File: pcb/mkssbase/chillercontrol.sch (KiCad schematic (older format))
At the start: 13 parts, among them J17 Switch, J18 PWR IN, J19 PWR OUT, J20 SSR, Q2 BC547, U2 4011

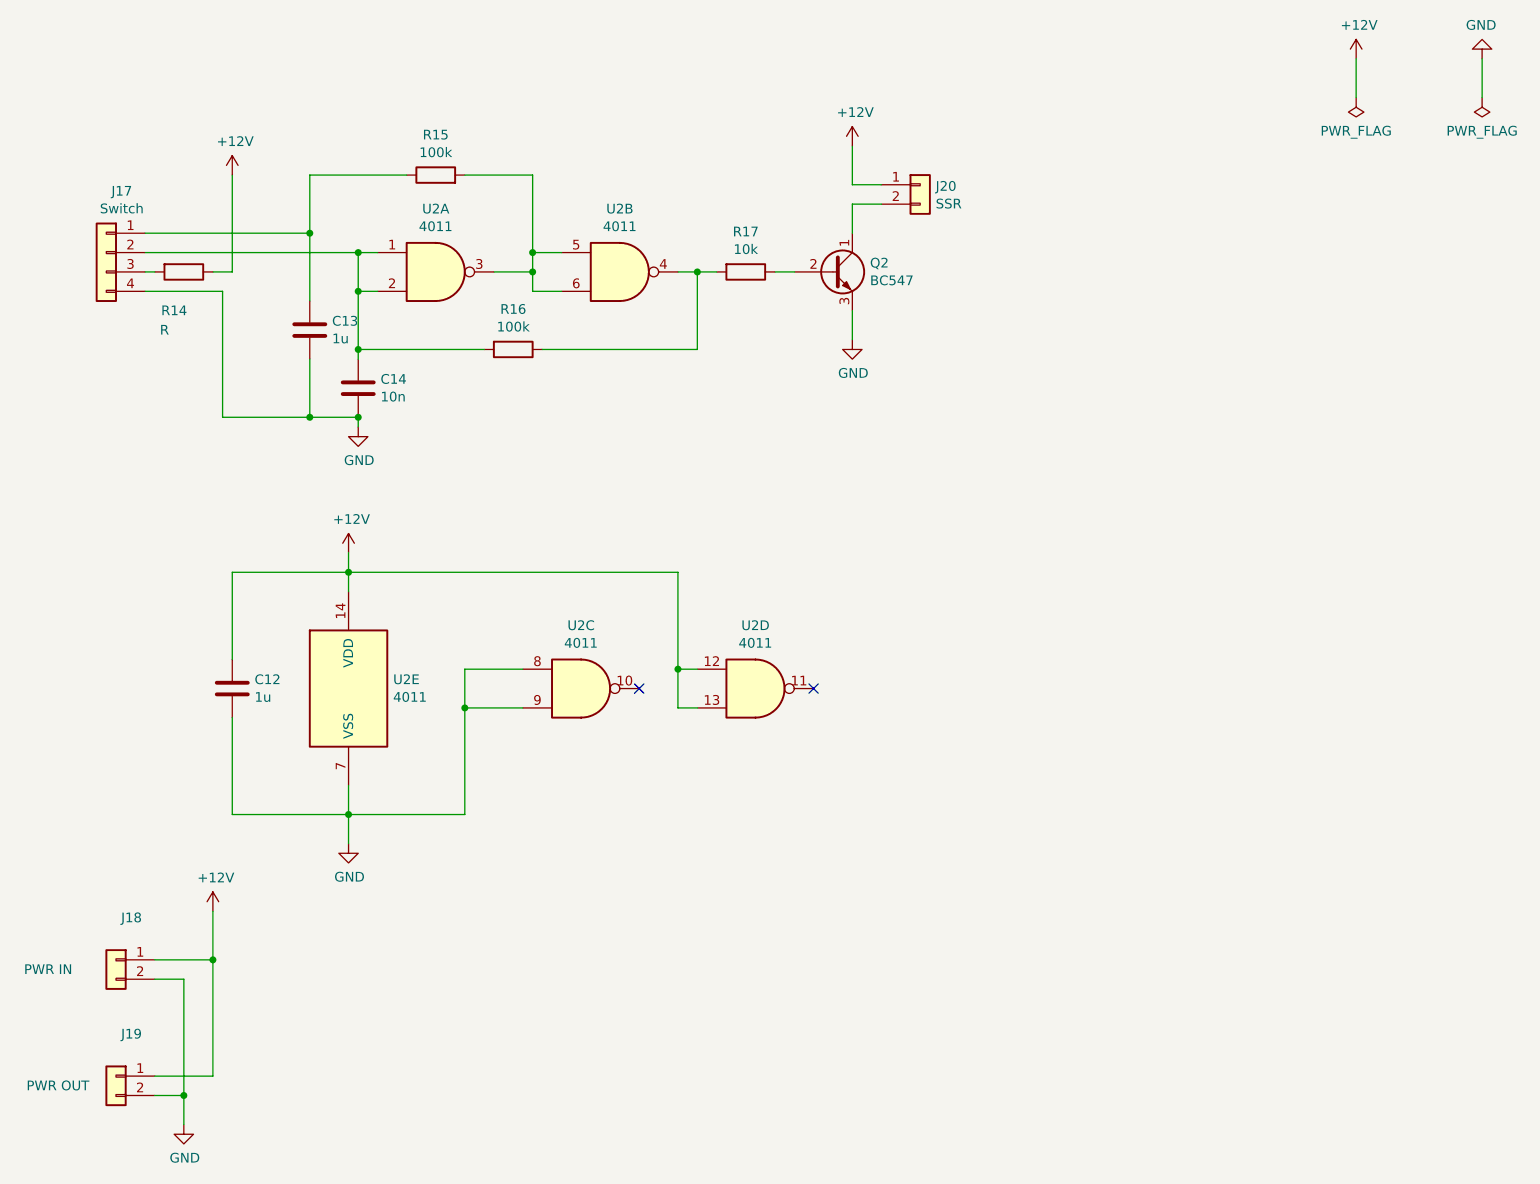
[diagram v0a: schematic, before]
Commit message: Integrate chiller control.
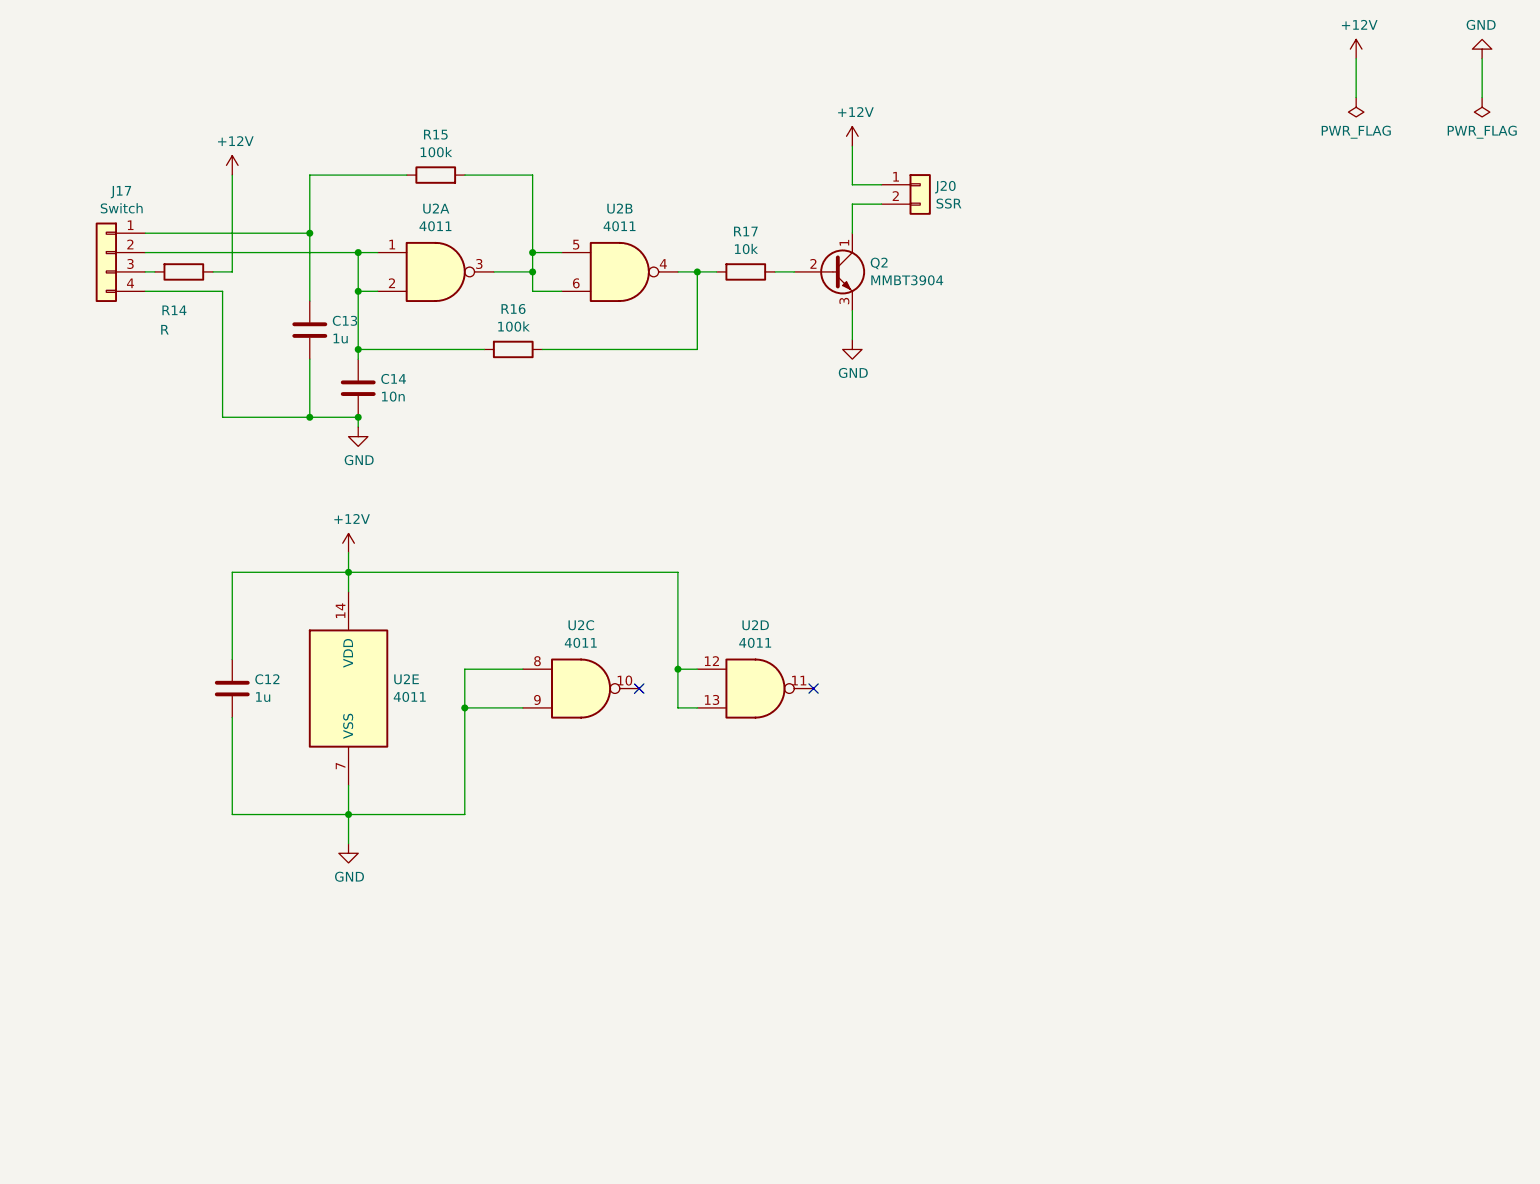
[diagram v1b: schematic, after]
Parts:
- removed J18: PWR IN, Connector_JST:JST_PH_B2B-PH-K_1x02_P2.00mm_Vertical, symbol Connector_Generic:Conn_01x02
- removed J19: PWR OUT, Connector_JST:JST_PH_B2B-PH-K_1x02_P2.00mm_Vertical, symbol Connector_Generic:Conn_01x02
- C12, C13: footprint Capacitor_THT:C_Rect_L7.0mm_W6.0mm_P5.00mm -> Capacitor_SMD:C_0805_2012Metric
- C14: footprint Capacitor_THT:C_Disc_D8.0mm_W2.5mm_P5.00mm -> Capacitor_SMD:C_0603_1608Metric
- Q2: value BC547 -> MMBT3904; footprint Package_TO_SOT_THT:TO-92L_Wide -> Package_TO_SOT_SMD:SOT-23
- R15, R16, R17: footprint Resistor_THT:R_Axial_DIN0207_L6.3mm_D2.5mm_P5.08mm_Vertical -> Resistor_SMD:R_0603_1608Metric
- U2: footprint Package_DIP:DIP-14_W7.62mm_LongPads -> Package_SO:SOIC-14_3.9x8.7mm_P1.27mm
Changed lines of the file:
@@
 EESchema Schematic File Version 4
 LIBS:mkssbase-cache
-LIBS:chillercontrol-cache
 EELAYER 26 0
 EELAYER END
@@
 $EndDescr
 $Comp
-L Connector_Generic:Conn_01x02 J19
-U 1 1 5C59E722
-P 1900 6950
-F 0 "J19" H 1820 7167 50  0000 C CNN
-F 1 "PWR OUT" H 2200 6900 50  0000 C CNN
-F 2 "Connector_JST:JST_PH_B2B-PH-K_1x02_P2.00mm_Vertical" H 1900 6950 50  0001 C CNN
-F 3 "~" H 1900 6950 50  0001 C CNN
-	1    1900 6950
-	-1   0    0    -1
-$EndComp
-$Comp
-L Connector_Generic:Conn_01x02 J18
-U 1 1 5C59E800
-P 1900 6350
-F 0 "J18" H 1820 6567 50  0000 C CNN
-F 1 "PWR IN" H 2250 6300 50  0000 C CNN
-F 2 "Connector_JST:JST_PH_B2B-PH-K_1x02_P2.00mm_Vertical" H 1900 6350 50  0001 C CNN
-F 3 "~" H 1900 6350 50  0001 C CNN
-	1    1900 6350
-	-1   0    0    -1
-$EndComp
-$Comp
 L Connector_Generic:Conn_01x02 J20
 U 1 1 5C59E879
@@
 F 0 "U2" H 4500 3125 50  0000 C CNN
 F 1 "4011" H 4500 3034 50  0000 C CNN
-F 2 "Package_DIP:DIP-14_W7.62mm_LongPads" H 4500 2800 50  0001 C CNN
+F 2 "Package_SO:SOIC-14_3.9x8.7mm_P1.27mm" H 4500 2800 50  0001 C CNN
 F 3 "http://www.intersil.com/content/dam/Intersil/documents/cd40/cd4011bms-12bms-23bms.pdf" H 4500 2800 50  0001 C CNN
 	2    4500 2800
@@
 F 0 "R15" V 3757 2300 50  0000 C CNN
 F 1 "100k" V 3666 2300 50  0000 C CNN
-F 2 "Resistor_THT:R_Axial_DIN0207_L6.3mm_D2.5mm_P5.08mm_Vertical" V 3480 2300 50  0001 C CNN
+F 2 "Resistor_SMD:R_0603_1608Metric" V 3480 2300 50  0001 C CNN
 F 3 "~" H 3550 2300 50  0001 C CNN
 	1    3550 2300
@@
 F 0 "R16" V 3743 3200 50  0000 C CNN
 F 1 "100k" V 3834 3200 50  0000 C CNN
-F 2 "Resistor_THT:R_Axial_DIN0207_L6.3mm_D2.5mm_P5.08mm_Vertical" V 3880 3200 50  0001 C CNN
+F 2 "Resistor_SMD:R_0603_1608Metric" V 3880 3200 50  0001 C CNN
 F 3 "~" H 3950 3200 50  0001 C CNN
 	1    3950 3200
@@
 F 0 "C14" H 3265 3446 50  0000 L CNN
 F 1 "10n" H 3265 3355 50  0000 L CNN
-F 2 "Capacitor_THT:C_Disc_D8.0mm_W2.5mm_P5.00mm" H 3188 3250 50  0001 C CNN
+F 2 "Capacitor_SMD:C_0603_1608Metric" H 3188 3250 50  0001 C CNN
 F 3 "~" H 3150 3400 50  0001 C CNN
 	1    3150 3400
@@
 F 0 "C13" H 3015 3146 50  0000 L CNN
 F 1 "1u" H 3015 3055 50  0000 L CNN
-F 2 "Capacitor_THT:C_Rect_L7.0mm_W6.0mm_P5.00mm" H 2938 2950 50  0001 C CNN
+F 2 "Capacitor_SMD:C_0805_2012Metric" H 2938 2950 50  0001 C CNN
 F 3 "~" H 2900 3100 50  0001 C CNN
 	1    2900 3100
@@
 F 0 "U2" H 3330 4996 50  0000 L CNN
 F 1 "4011" H 3330 4905 50  0000 L CNN
-F 2 "Package_DIP:DIP-14_W7.62mm_LongPads" H 3100 4950 50  0001 C CNN
+F 2 "Package_SO:SOIC-14_3.9x8.7mm_P1.27mm" H 3100 4950 50  0001 C CNN
 F 3 "http://www.intersil.com/content/dam/Intersil/documents/cd40/cd4011bms-12bms-23bms.pdf" H 3100 4950 50  0001 C CNN
 	5    3100 4950
@@
 F 0 "U2" H 4300 5275 50  0000 C CNN
 F 1 "4011" H 4300 5184 50  0000 C CNN
-F 2 "Package_DIP:DIP-14_W7.62mm_LongPads" H 4300 4950 50  0001 C CNN
+F 2 "Package_SO:SOIC-14_3.9x8.7mm_P1.27mm" H 4300 4950 50  0001 C CNN
 F 3 "http://www.intersil.com/content/dam/Intersil/documents/cd40/cd4011bms-12bms-23bms.pdf" H 4300 4950 50  0001 C CNN
 	3    4300 4950
@@
 F 0 "U2" H 5200 5275 50  0000 C CNN
 F 1 "4011" H 5200 5184 50  0000 C CNN
-F 2 "Package_DIP:DIP-14_W7.62mm_LongPads" H 5200 4950 50  0001 C CNN
+F 2 "Package_SO:SOIC-14_3.9x8.7mm_P1.27mm" H 5200 4950 50  0001 C CNN
 F 3 "http://www.intersil.com/content/dam/Intersil/documents/cd40/cd4011bms-12bms-23bms.pdf" H 5200 4950 50  0001 C CNN
 	4    5200 4950
@@
 F 0 "C12" H 2615 4996 50  0000 L CNN
 F 1 "1u" H 2615 4905 50  0000 L CNN
-F 2 "Capacitor_THT:C_Rect_L7.0mm_W6.0mm_P5.00mm" H 2538 4800 50  0001 C CNN
+F 2 "Capacitor_SMD:C_0805_2012Metric" H 2538 4800 50  0001 C CNN
 F 3 "~" H 2500 4950 50  0001 C CNN
 	1    2500 4950
@@
 P 5600 2800
 F 0 "Q2" H 5791 2846 50  0000 L CNN
-F 1 "BC547" H 5791 2755 50  0000 L CNN
-F 2 "Package_TO_SOT_THT:TO-92L_Wide" H 5800 2725 50  0001 L CIN
+F 1 "MMBT3904" H 5791 2755 50  0000 L CNN
+F 2 "Package_TO_SOT_SMD:SOT-23" H 5800 2725 50  0001 L CIN
 F 3 "http://www.fairchildsemi.com/ds/BC/BC547.pdf" H 5600 2800 50  0001 L CNN
 	1    5600 2800
@@
 F 0 "R17" V 4943 2800 50  0000 C CNN
 F 1 "10k" V 5034 2800 50  0000 C CNN
-F 2 "Resistor_THT:R_Axial_DIN0207_L6.3mm_D2.5mm_P5.08mm_Vertical" V 5080 2800 50  0001 C CNN
+F 2 "Resistor_SMD:R_0603_1608Metric" V 5080 2800 50  0001 C CNN
 F 3 "~" H 5150 2800 50  0001 C CNN
 	1    5150 2800
@@
 Wire Wire Line
 	5700 2350 5850 2350
-$Comp
-L power:+12V #PWR06
-U 1 1 5C5A674F
-P 2400 6100
-F 0 "#PWR06" H 2400 5950 50  0001 C CNN
-F 1 "+12V" H 2415 6273 50  0000 C CNN
-F 2 "" H 2400 6100 50  0001 C CNN
-F 3 "" H 2400 6100 50  0001 C CNN
-	1    2400 6100
-	1    0    0    -1
-$EndComp
-Wire Wire Line
-	2400 6100 2400 6350
-Wire Wire Line
-	2400 6350 2100 6350
-Wire Wire Line
-	2400 6350 2400 6950
-Wire Wire Line
-	2400 6950 2100 6950
-Connection ~ 2400 6350
-$Comp
-L power:GND #PWR01
-U 1 1 5C5A94A2
-P 2250 7200
-F 0 "#PWR01" H 2250 6950 50  0001 C CNN
-F 1 "GND" H 2255 7027 50  0000 C CNN
-F 2 "" H 2250 7200 50  0001 C CNN
-F 3 "" H 2250 7200 50  0001 C CNN
-	1    2250 7200
-	1    0    0    -1
-$EndComp
-Wire Wire Line
-	2100 6450 2250 6450
-Wire Wire Line
-	2250 6450 2250 7050
-Wire Wire Line
-	2100 7050 2250 7050
-Connection ~ 2250 7050
-Wire Wire Line
-	2250 7050 2250 7200
 $Comp
 L power:PWR_FLAG #FLG01
@@
 F 0 "U2" H 3550 3125 50  0000 C CNN
 F 1 "4011" H 3550 3034 50  0000 C CNN
-F 2 "Package_DIP:DIP-14_W7.62mm_LongPads" H 3550 2800 50  0001 C CNN
+F 2 "Package_SO:SOIC-14_3.9x8.7mm_P1.27mm" H 3550 2800 50  0001 C CNN
 F 3 "http://www.intersil.com/content/dam/Intersil/documents/cd40/cd4011bms-12bms-23bms.pdf" H 3550 2800 50  0001 C CNN
 	1    3550 2800
